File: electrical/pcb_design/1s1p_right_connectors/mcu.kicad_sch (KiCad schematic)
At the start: 20 parts, among them J17 STLINK_TagConnect_6, U1 BMI323, U2 BMI323, U4 STM32L452CEU6

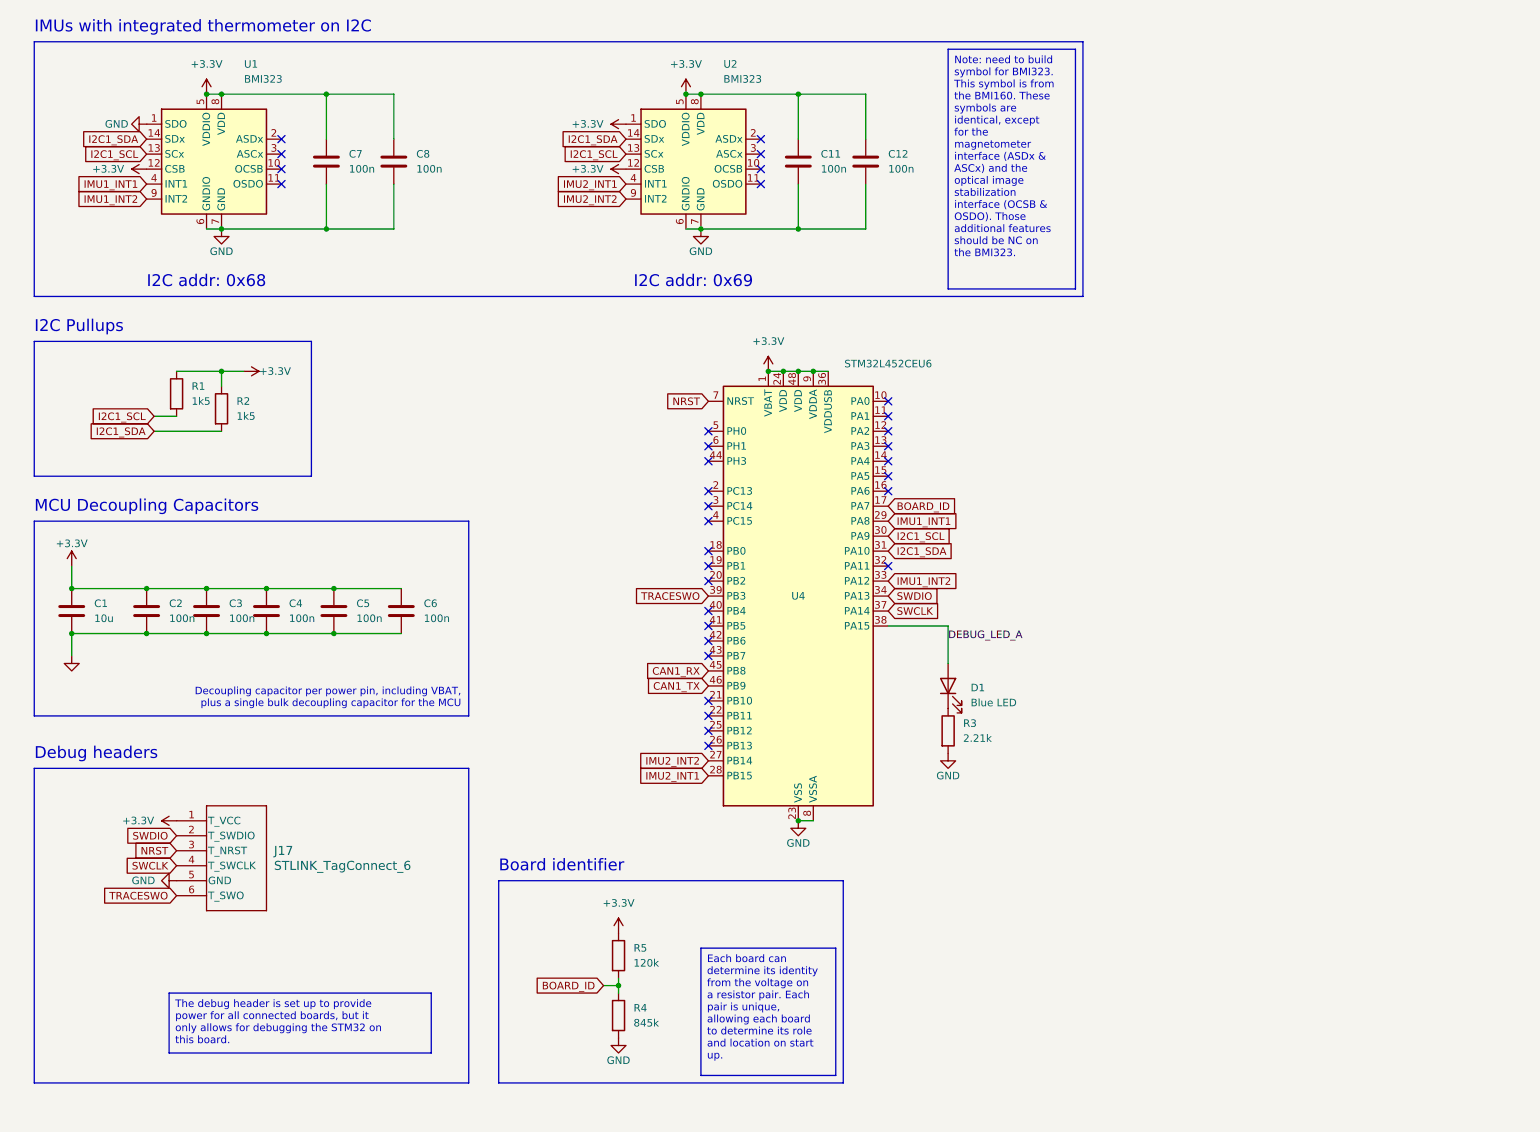
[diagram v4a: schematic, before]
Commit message: Incorporated feedback on schematic and pcb for one board. Next step will be to translate this to the other boards.
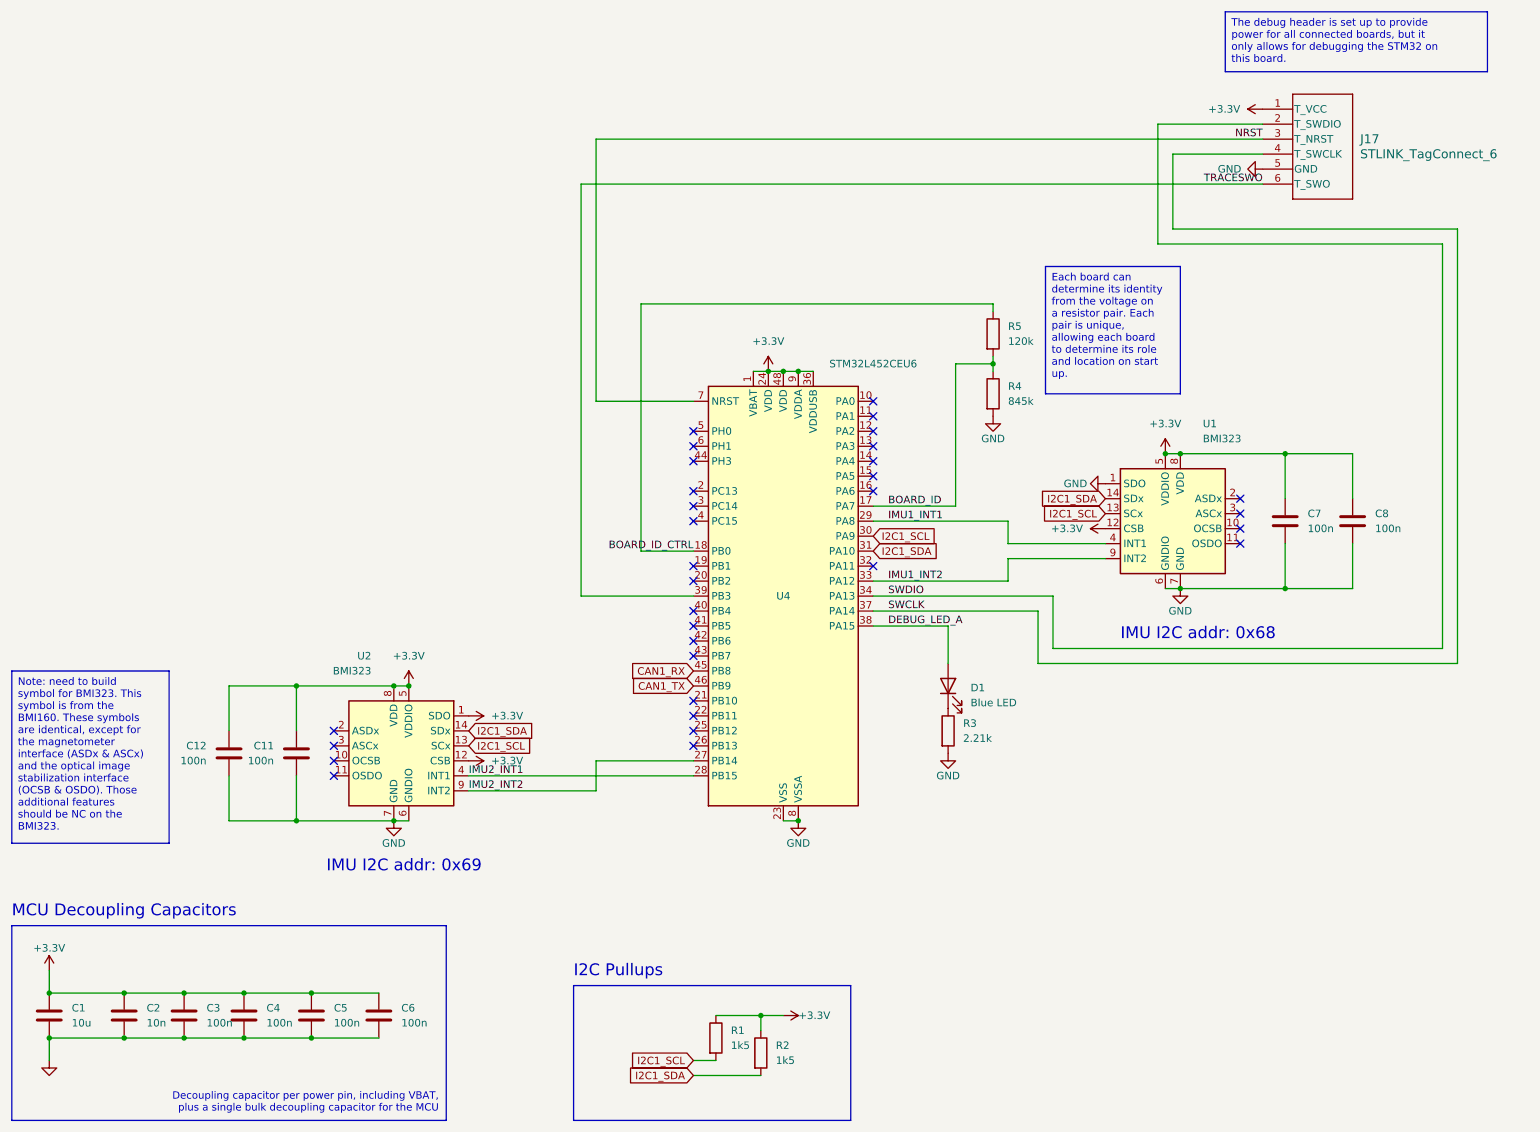
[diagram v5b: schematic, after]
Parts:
- C2: value 100n -> 10n; MPN C2649549 -> C5189696; Manufacturer Part Number GCM155R71H104KE02J -> GCM155R71H103JA55D
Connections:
- net +3.3V: no longer R5.1
- net BOARD_ID_CTRL: now reaches U4.18 (PB0)
- net BOARD_ID_CTRL: now also R5.1
- no-connect marks 33 -> 32
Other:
- note added: "IMU I2C addr: 0x68"
- note added: "IMU I2C addr: 0x69"
- note removed: "Board identifier"
- note removed: "Debug headers"
- note removed: "I2C addr: 0x68"
- note removed: "I2C addr: 0x69"
- note removed: "IMUs with integrated thermometer on I2C"
- moved on the sheet: C1, C11, C12, C2, C3, C4, C5, C6, C7, C8, J17, R1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
